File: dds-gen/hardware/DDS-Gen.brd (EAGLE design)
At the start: 100 x 80 mm, 36 parts, among them IC1 TL072P, J1 POWER, J2 AVR_SPI_PROG_3X2PTH, J3 I2C CTRL, J4 BNCPTH, Q1 30MHz, U1 ATMEGA328P-PU

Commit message: Updates begin layout of board, switched to ganged resistors
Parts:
- removed R10, R11, R3, R4, R5, R6, R7, R8, R9: 20k, rcl:0204/5
- removed R12, R13, R14, R15, R16, R17, R18: 10k, rcl:0204/5
- added R23, R24, R25, R26, R27, R28, R29: 10k, rcl:0204/5
- added RN1, RN2, RN3, RN4: 10k, resistor-sil:SIL10
- R21: device rcl:0204/5 -> resistor:0204/7
- moved R21 165.9 mm to (68.6, 12.7)
- moved J4 162.6 mm to (91.4, 7.62), turned to 180 degrees
- moved R20 132.2 mm to (57.1, 54.6), turned to 90 degrees
- moved R19 121.1 mm to (54.6, 59.7), turned to 90 degrees
- moved C6 113.0 mm to (58.4, 25.4), turned to 90 degrees
- moved R2 108.9 mm to (22.9, 20.3), turned to 180 degrees
- moved R22 107.4 mm to (69.8, 2.54)
- moved R1 100.5 mm to (64.8, 39.4), turned to 180 degrees
- moved S1 99.4 mm to (25.4, 14.0), turned to 90 degrees
- moved IC1 96.6 mm to (66.0, 22.9), turned to 180 degrees
- moved C2 93.2 mm to (34.3, 49.5), turned to 180 degrees
- moved J2 90.2 mm to (11.4, 52.1), turned to 90 degrees
- moved C1 88.9 mm to (34.3, 44.5), turned to 180 degrees
- moved U1 86.1 mm to (15.2, 59.7), turned to 180 degrees
- moved C4 78.1 mm to (26.7, 22.9)
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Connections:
- removed net N$13: R17.2, R18.1, R9.1
- removed net N$14: R16.2, R17.1, R8.1
- removed net N$15: R15.2, R16.1, R7.1
- removed net N$16: R14.2, R15.1, R6.1
- removed net N$17: R13.2, R14.1, R5.1
- removed net N$18: R12.2, R13.1, R4.1
- removed net N$19: R11.2, R12.1, R3.1
- removed net N$20: R10.1, R18.2, R19.2
- new net N$25: RN1.1, RN3.1
- new net N$26: RN1.3, RN3.3
- new net N$27: RN1.5, RN3.5
- new net N$28: RN1.7, RN3.7
- new net N$29: RN1.9, RN3.9
- new net N$30: RN2.1, RN4.1
- new net N$31: RN2.3, RN4.3
- new net N$32: RN2.5, RN4.5
- new net N$33: RN2.7, RN4.7
- new net N$34: R23.1, RN4.6, RN4.8
- new net N$35: R23.2, R24.1, RN4.4
- new net N$36: R24.2, R25.1, RN4.2
- new net N$37: R25.2, R26.1, RN3.10
- new net N$38: R26.2, R27.1, RN3.8
- new net N$39: R27.2, R28.1, RN3.6
- new net N$40: R28.2, R29.1, RN3.4
- new net N$41: R19.2, R29.2, RN3.2
- net 0V: now also RN2.8; no longer R11.1
- net N$10: now also RN2.2, U1.4; no longer R8.2, U1.11
- net N$11: now also RN2.4, U1.3; no longer R9.2, U1.12
- net N$12: now also RN2.6, U1.2; no longer R10.2, U1.13
- net N$5: now also RN1.2, U1.13; no longer R3.2, U1.2
- net N$6: now also RN1.4, U1.12; no longer R4.2, U1.3
- net N$7: now also RN1.6, U1.11; no longer R5.2, U1.4
- net N$8: now also RN1.8, U1.6; no longer R6.2, U1.5
- net N$9: now also RN1.10, U1.5; no longer R7.2, U1.6
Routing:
- net 0V: track 0.00 -> 177.1 mm
- net +5V: track 0.00 -> 69.8 mm, vias 0 -> 2
- net N$23: track 0.00 -> 43.1 mm
- net N$8: track 0.00 -> 27.9 mm
- net N$9: track 0.00 -> 25.4 mm
- net N$5: track 0.00 -> 25.4 mm
- net RESET: track 0.00 -> 23.9 mm
- net N$6: track 0.00 -> 22.9 mm
- net N$12: track 0.00 -> 22.9 mm
- net N$10: track 0.00 -> 22.9 mm
- net N$22: track 0.00 -> 21.6 mm
- net N$7: track 0.00 -> 20.3 mm
- net N$11: track 0.00 -> 20.3 mm
- net N$21: track 0.00 -> 16.5 mm
- net N$1: track 0.00 -> 12.7 mm
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
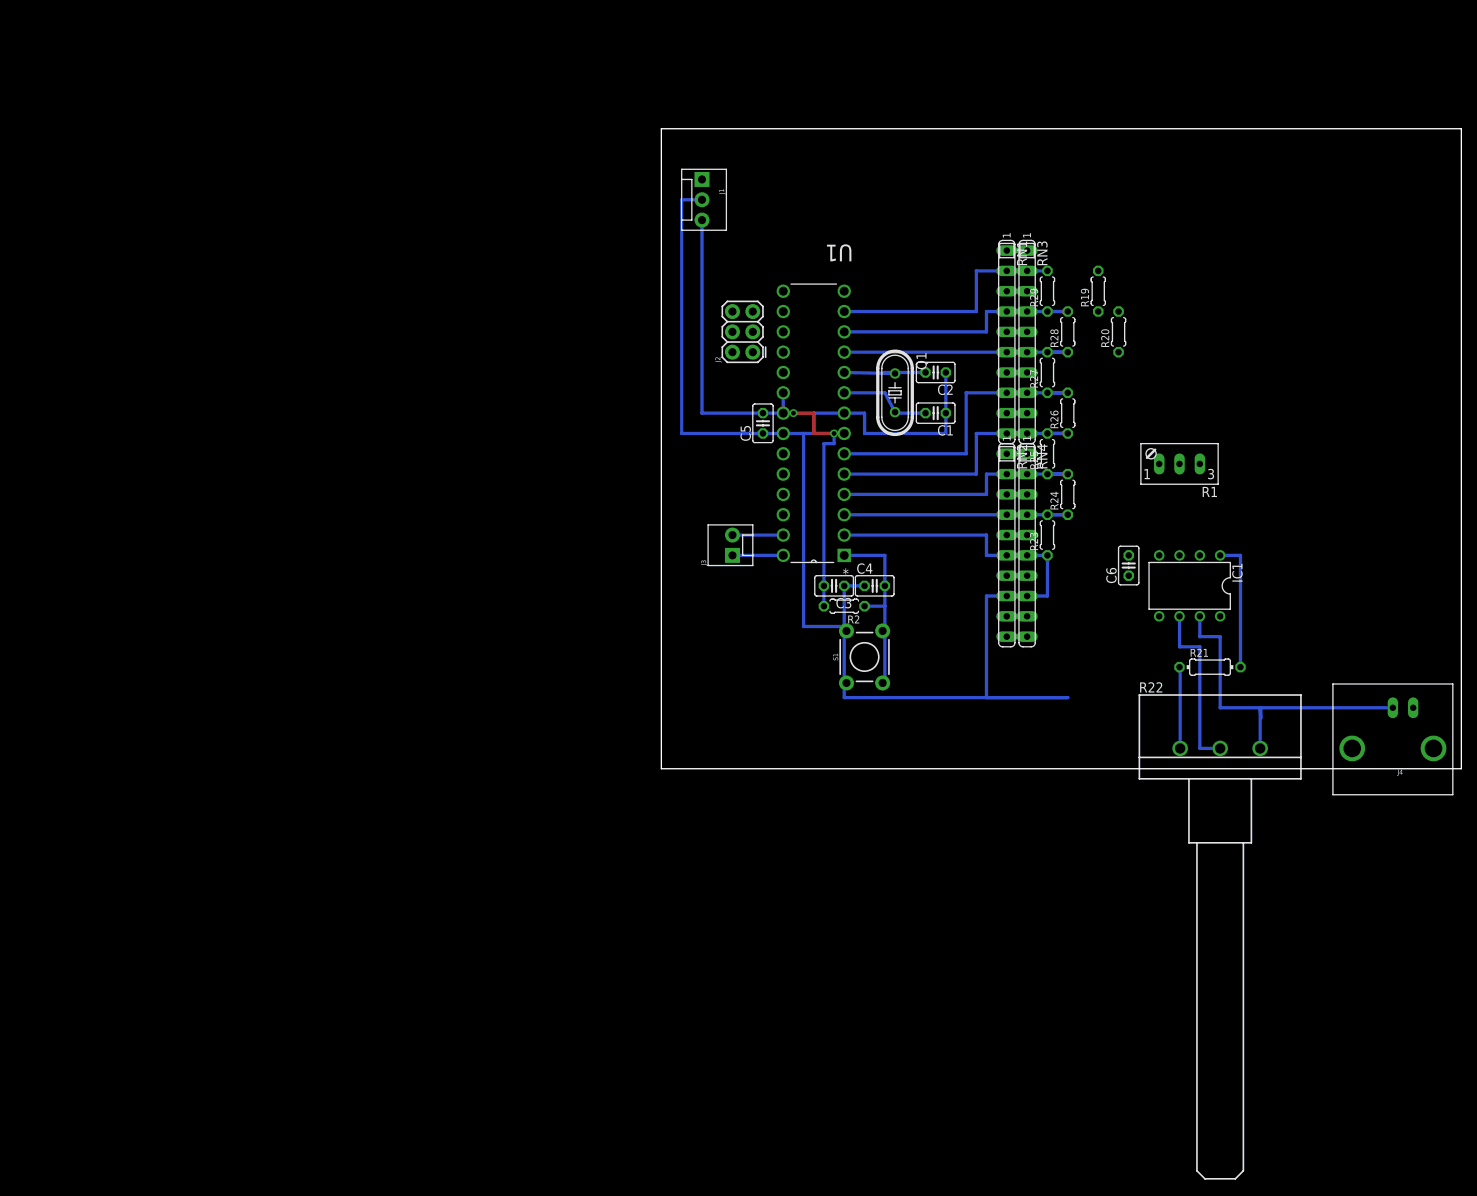
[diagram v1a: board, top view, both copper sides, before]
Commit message: Layout tweaks and offset control.
Added switchable offset control to output amplifier. Can be switched in or out.
Tweak to layout so pots work in a natual manner (eg clockwise to increase amplitude)
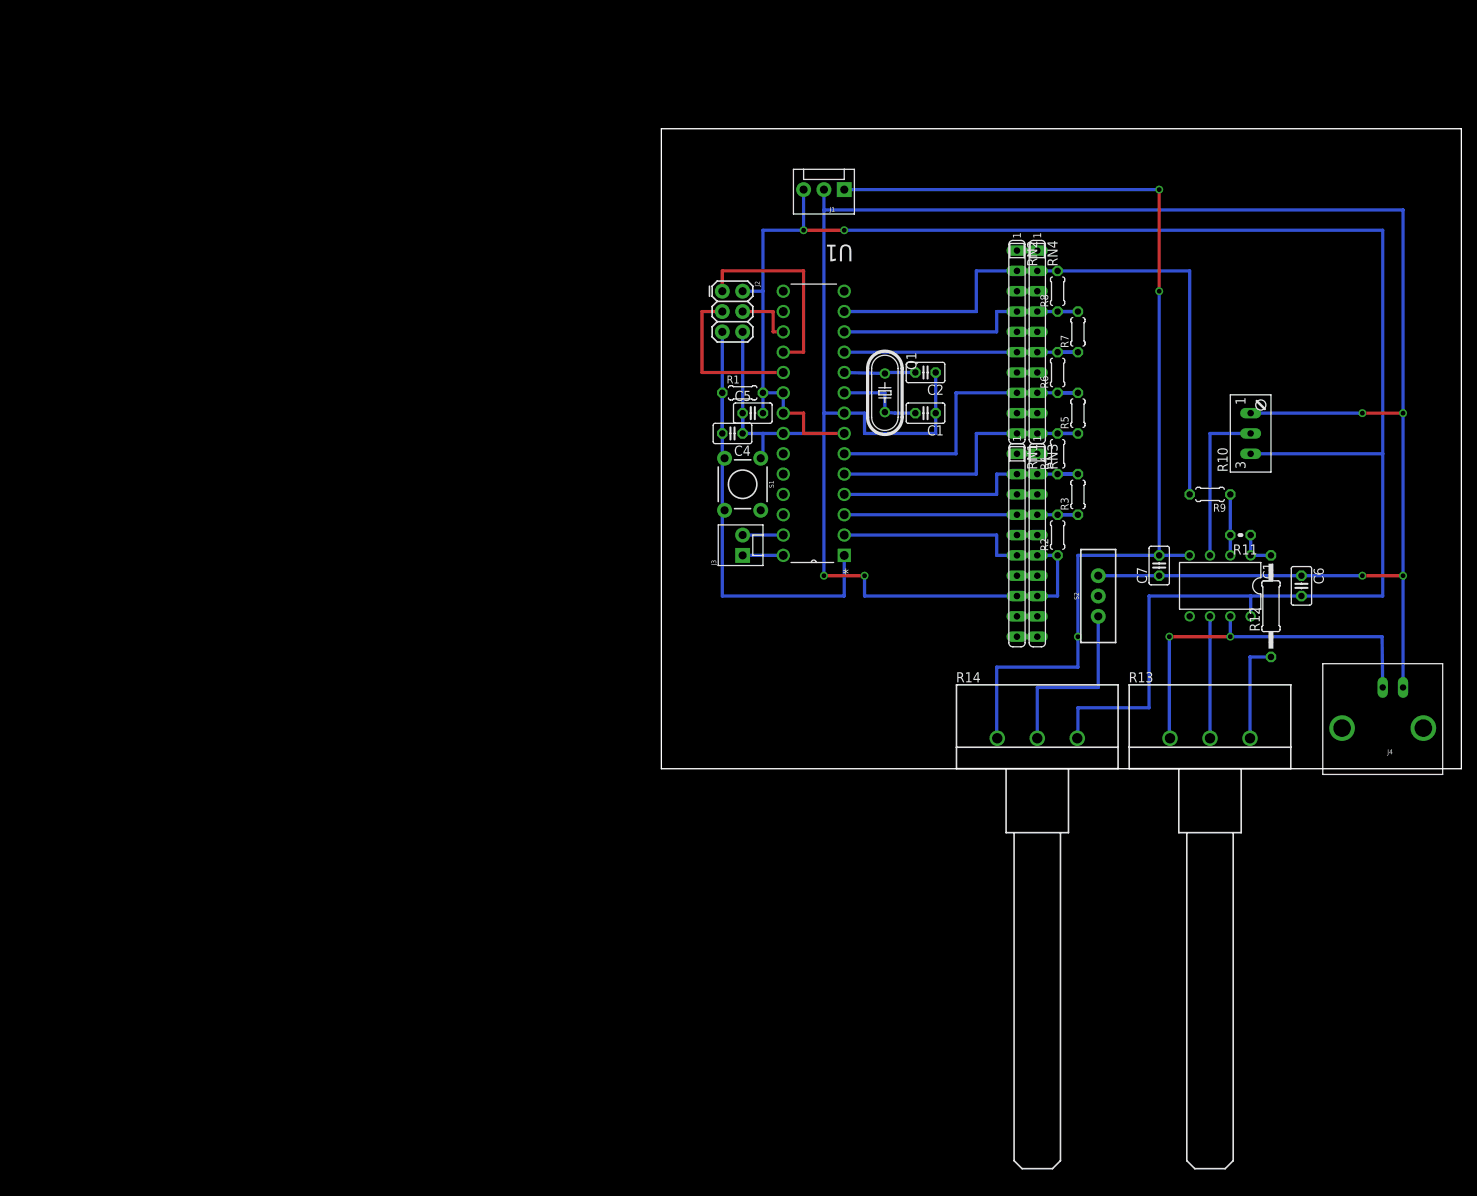
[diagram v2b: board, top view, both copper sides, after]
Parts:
- removed C3: 0.1uF, rcl:C025-025X050
- removed R19, R20: 100k, rcl:0204/5
- removed R21: 100, resistor:0204/7
- removed R22: 10k, pot:CIP20C-6MM
- removed R23, R24, R25, R26, R27, R28, R29: 10k, rcl:0204/5
- added C7: 0.1uF, rcl:C025-025X050
- added R10: 1k, pot:S64W
- added R11: 100k, rcl:0204V
- added R12: 100, rcl:0207/12
- added R13, R14: 10k, pot:CIP20C-6MM
- added R3, R4, R5, R6, R7, R8: 10k, rcl:0204/5
- added R9: 100k, rcl:0204/5
- added S2: (no value), SparkFun-Switches:SWITCH_SPDT_PTH_11.6X4.0MM
- R1: value 1k -> 10k; device pot:S64W -> rcl:0204/5
- moved R1 55.1 mm to (10.2, 47.0), turned to 0 degrees
- moved R2 28.1 mm to (49.5, 29.2), turned to 90 degrees
- moved S1 26.4 mm to (10.2, 35.6), turned to 270 degrees
- moved C4 26.1 mm to (8.89, 41.9), turned to 180 degrees
- moved RN1 25.4 mm to (44.5, 27.9)
- moved RN2 25.4 mm to (44.5, 53.3)
- moved RN3 25.4 mm to (47.0, 27.9)
- moved RN4 25.4 mm to (47.0, 53.3)
- moved C6 21.7 mm to (80.0, 22.9), turned to 270 degrees
- moved J1 17.8 mm to (22.9, 72.4), turned to 180 degrees
- moved J2 8.52 mm to (7.62, 59.7), turned to 270 degrees
- moved IC1 3.81 mm to (69.8, 22.9)
- moved J4 2.84 mm to (90.2, 10.2)
- moved C5 1.80 mm to (11.4, 44.5), turned to 0 degrees
- moved J3 1.27 mm to (10.2, 26.7)
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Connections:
- removed net N$24: R21.1, R22.A
- new net N$13: IC1.5, S2.2
- new net N$15: R14.S, S2.3
- new net N$16: R12.1, R13.E
- net +5V: now also C6.2, R1.2, R10.E, R14.E; no longer C3.2, R1.E, R2.2
- net -5V: now also C7.2, R14.A; no longer C6.2
- net 0V: now also C7.1, R10.A, RN1.8, S2.1; no longer C3.1, IC1.5, R1.A, RN2.8
- net N$10: now also RN1.2; no longer RN2.2
- net N$11: now also RN1.4; no longer RN2.4
- net N$12: now also RN1.6; no longer RN2.6
- net N$21: now also R11.1, R12.2; no longer R20.1, R21.2
- net N$22: now also R13.S; no longer R22.S
- net N$23: now also R13.A; no longer R22.E
- net N$29: now also RN2.9, RN4.9; no longer RN1.9, RN3.9
- net N$3: now also R10.S; no longer R1.S
- net N$34: now also R2.1, RN3.6, RN3.8; no longer R23.1, RN4.6, RN4.8
- net N$35: now also R2.2, R3.1, RN3.4; no longer R23.2, R24.1, RN4.4
- net N$36: now also R3.2, R4.1, RN3.2; no longer R24.2, R25.1, RN4.2
- net N$37: now also R4.2, R5.1, RN4.10; no longer R25.2, R26.1, RN3.10
- net N$38: now also R5.2, R6.1, RN4.8; no longer R26.2, R27.1, RN3.8
- net N$39: now also R6.2, R7.1, RN4.6; no longer R27.2, R28.1, RN3.6
- net N$4: now also R11.2, R9.1; no longer R19.1, R20.2
- net N$40: now also R7.2, R8.1, RN4.4; no longer R28.2, R29.1, RN3.4
- net N$41: now also R8.2, R9.2, RN4.2; no longer R19.2, R29.2, RN3.2
- net N$5: now also RN2.2; no longer RN1.2
- net N$6: now also RN2.4; no longer RN1.4
- net N$7: now also RN2.6; no longer RN1.6
- net N$8: now also RN2.8; no longer RN1.8
- net N$9: now also RN2.10; no longer RN1.10
- net RESET: now also R1.1; no longer R2.1
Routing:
- net +5V: track 69.8 -> 243.9 mm
- net 0V: track 177.1 -> 317.1 mm, vias 0 -> 6
- net -5V: track 0.00 -> 132.2 mm, vias 0 -> 3
- net N$41: track 2.54 -> 47.0 mm
- net RESET: track 23.9 -> 58.7 mm
- net MISO: track 0.00 -> 25.4 mm
- net N$15: track 0.00 -> 22.9 mm
- net SCK: track 0.00 -> 20.3 mm
- net N$3: track 0.00 -> 20.3 mm
- net N$16: track 0.00 -> 12.8 mm
- net N$21: track 16.5 -> 5.08 mm
- net N$24: track 10.2 -> 0.00 mm
- net MOSI: track 0.00 -> 7.62 mm
- net N$4: track 0.00 -> 7.62 mm
- net N$22: track 21.6 -> 15.2 mm
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
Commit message: Updated Schematic with slit power supply +-9V and 5V
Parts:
- J1: value POWER -> (none); device SparkFun-Connectors:MOLEX-1X3 -> SparkFun-Connectors:MOLEX-1X6
- moved J1 18.3 mm to (7.62, 62.2), turned to 90 degrees
- moved J2 2.54 mm to (7.62, 57.1)
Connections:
- removed net +5V: C5.2, C6.2, IC1.8, J1.3, J2.2, R1.2, R10.E, R14.E, U1.20, U1.21, U1.7
- removed net -5V: C7.2, IC1.4, J1.1, R14.A
- new net +9V: C6.2, IC1.8, J1.4, R10.E, R14.E
- new net -9V: C7.2, IC1.4, J1.6, R14.A
- new net VCC: C5.2, J1.1, R1.2, U1.20, U1.21, U1.7
- net 0V: now also J1.3, J1.5
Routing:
- net +5V: track 243.9 -> 0.00 mm, vias 2 -> 0
- net +9V: track 0.00 -> 205.8 mm
- net -9V: track 0.00 -> 149.9 mm, vias 0 -> 3
- net -5V: track 132.2 -> 0.00 mm, vias 3 -> 0
- net VCC: track 0.00 -> 45.7 mm
- net 0V: track 317.1 -> 347.5 mm
- net N$13: track 0.00 -> 14.0 mm
- net SCK: track 20.3 -> 17.8 mm
- net MOSI: track 7.62 -> 5.08 mm
- net RESET: track 58.7 -> 56.2 mm
